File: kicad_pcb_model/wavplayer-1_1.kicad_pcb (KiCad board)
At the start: 2 copper layers, 34 x 77.2 mm, 14 parts, among them SW1 DOWN, SW2 BACK, SW3 UP, SW4 ENTER

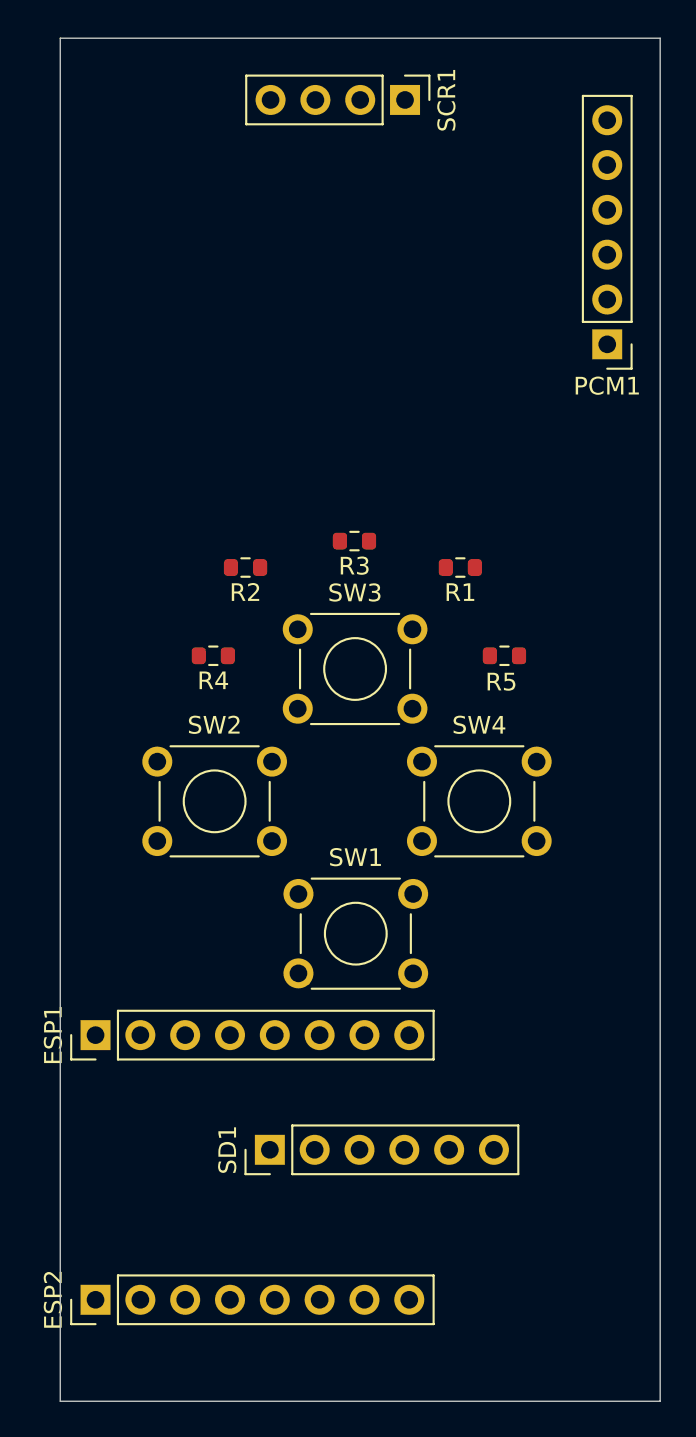
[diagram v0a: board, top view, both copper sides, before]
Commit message: added new tracings, gbr files
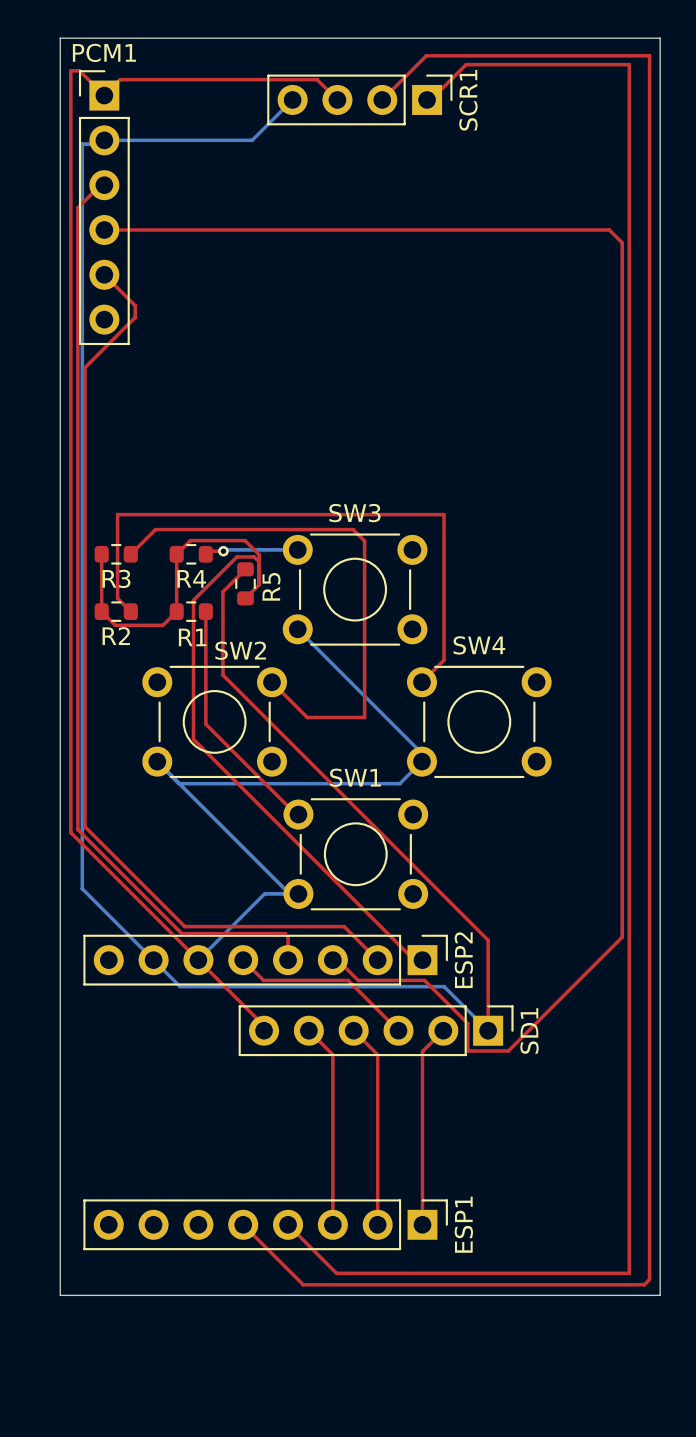
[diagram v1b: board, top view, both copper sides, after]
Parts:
- moved PCM1 31.8 mm to (122.5, 53.8), turned to 0 degrees
- moved ESP2 26.7 mm to (140.5, 102.8), turned to -90 degrees
- moved ESP1 21.4 mm to (140.5, 117.8), turned to -90 degrees
- moved R1 15.5 mm to (127.4, 83.0)
- moved R5 15.2 mm to (130.5, 81.4), turned to -90 degrees
- moved SD1 14.1 mm to (144.2, 106.8), turned to -90 degrees
- moved R3 13.5 mm to (123.2, 79.8)
- moved R2 7.74 mm to (123.2, 83.0)
- moved R4 5.88 mm to (127.4, 79.8)
- moved SW1 4.50 mm to (133.5, 94.5)
- moved SW2 4.50 mm to (125.5, 87.0)
- moved SW3 4.50 mm to (133.5, 79.5)
- moved SW4 4.50 mm to (140.5, 87.0)
- moved SCR1 1.25 mm to (140.8, 54.0)
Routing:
- net +3V3: track 0.78 -> 120.3 mm
- net GND: track 0.00 -> 114.4 mm
- net /SCL: track 0.65 -> 110.1 mm
- net /SDA: track 0.00 -> 101.3 mm
- net /GP2_ADC1_2: track 0.00 -> 91.1 mm
- net /GP3_ADC1_3: track 0.00 -> 53.1 mm
- net /GP1_ADC1_1: track 0.00 -> 52.9 mm
- net /GP0_ADC1_0: track 0.00 -> 51.7 mm
- net Net-(R2-Pad1): track 0.00 -> 34.3 mm
- net Net-(R3-Pad1): track 0.00 -> 30.2 mm
- net Net-(R1-Pad1): track 0.00 -> 13.7 mm
- net /MOSI: track 0.00 -> 11.6 mm
- net /CS: track 0.00 -> 11.6 mm
- net /MISO: track 0.00 -> 11.5 mm
- net /SCK: track 0.00 -> 10.5 mm
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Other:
- board size 34 x 77.2 mm -> 34 x 71.2 mm
- board text added: "PCM5102A BCK GPIO1 ACD1_1 (1) Sch T2 PCM5102A LRCK GPIO2 ACD1_2 (2) Sch T3 PCM5102A DATA GPIO3 ACD1_3 (3) Sch T4 PCM5102A 3.3V 3.3V PCM5102A GND GND SD SCK GPIO4 A4 / SCK (4) Sch T5 SD MISO GPIO5 A5 / MISO (21) Sch B1 SD MOSI GPIO6 MOSI (20) Sch B2 SD CS GPIO7 SS/CS (10) Sch B3 SSD1306 SDA GPIO8 SDA (9) Sch B4 SSD1306 SCL GPIO9 SCL (8) Sch B5"
